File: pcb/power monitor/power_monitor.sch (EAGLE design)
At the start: 23 parts

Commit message: Signed-off-by: timcronin <tmpcronin@gmail.com>
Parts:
- removed C2: 10 uF, rcl:C-USC0805
- removed C3: 10 nF, rcl:C-USC0402
- removed C4: 22 uF, rcl:C-USC1206
- removed C5: 22 uF, rcl:C-USC0402
- removed C6: 100 nF, rcl:C-USC0402
- removed J1: (no value), con-jack:DCJ0303
- removed R1: 10K, rcl:R-US_R0603
- removed R5, R6: 500K, rcl:R-US_R0603
- removed U$1: MOMO-EDGE-SMALL-M, components:MOMO-EDGE-SMALL-M
- removed U$2: MOMO-EDGE-SMALL-F, components:MOMO-EDGE-SMALL-F
- removed U$3: MOMO-EDGE-POWER-M, components:MOMO-EDGE-POWER-M
- removed U$4: MOMO-EDGE-POWER-F, components:MOMO-EDGE-POWER-F
- removed U$8: 4.7 uH, components:NR6028-INDUCTOR
- removed U$9: MCP1702, components:MCP1702
- added IC1, IC2, IC3: MAX4105ESA, maxim:MAX4105ESA
- added R7: 1k, rcl:R-US_R0603
- added R8: 69.8k, rcl:R-US_R0603
- R2: value 100K -> 2
- R3: value 50K 1% -> 69.8k
- R4: value 13K 1% -> 1k
- U$6: value XRP7659 -> MOMO-EDGE-8F; device components:XRP7659 -> components:MOMO-EDGE-8F
- U$7: value DIODE_SS2P3 -> MOMO-EDGE-8M; device components:DIODE_SS2P3 -> components:MOMO-EDGE-8M
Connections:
- removed net +12V: C2.1, J1.1, R2.1, U$6.VIN
- removed net N$5: C6.1, R5.1, R6.2, U$5.RA4/AN3
- removed net N$6: R3.1, R4.2, U$6.FB
- new net N$11: IC2G$1.+IN, R2.1, U$7.2.8V
- new net N$7: IC3G$1.-IN, R3.2, R4.1
- new net N$9: IC3G$1.+IN, R7.1, R8.2
- net CLK: now also U$6.CLK, U$7.CLK; no longer U$1.SCL, U$2.SCL
- net DAT: now also U$6.DAT, U$7.DAT; no longer U$1.SDA, U$2.SDA
- net GND: now also IC1P.VEE, IC2P.VEE, IC3P.VEE, R8.1, U$6.PGND, U$7.GND, U$7.PGND; no longer C2.2, C4.2, C5.2, C6.2, J1.2, J1.3, R4.1, R6.1, U$1.GND, U$2.GND, U$7.AN, U$9.GND
- net IRQ: now also U$6.ALRM, U$7.ALRM; no longer U$1.IRQ, U$2.IRQ
- net N$1: now also U$6.NC, U$7.NC; no longer R1.2
- net N$2: now also IC3G$1.OUT, R3.1, U$5.RA4/AN3; no longer C3.2, U$6.SW, U$7.CATH, U$8.1
- net N$3: now also IC2G$1.-IN, IC2G$1.OUT, R4.2; no longer R2.2, U$6.EN
- net N$4: now also IC1G$1.-IN, IC1G$1.OUT, R7.2; no longer C3.1, U$6.BS
- net V+: now also IC3P.VCC, U$6.4V, U$7.4V; no longer C4.1, R3.2, R5.2, U$3.3.8V, U$4.3.8V, U$8.2, U$9.VIN
- net VCCINT: now also IC1G$1.+IN, IC1P.VCC, IC2P.VCC, R2.2, U$6.2.8V; no longer C5.1, R1.1, U$1.2.8V, U$2.2.8V, U$9.VOUT
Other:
- moved on the sheet: R2, R3, R4

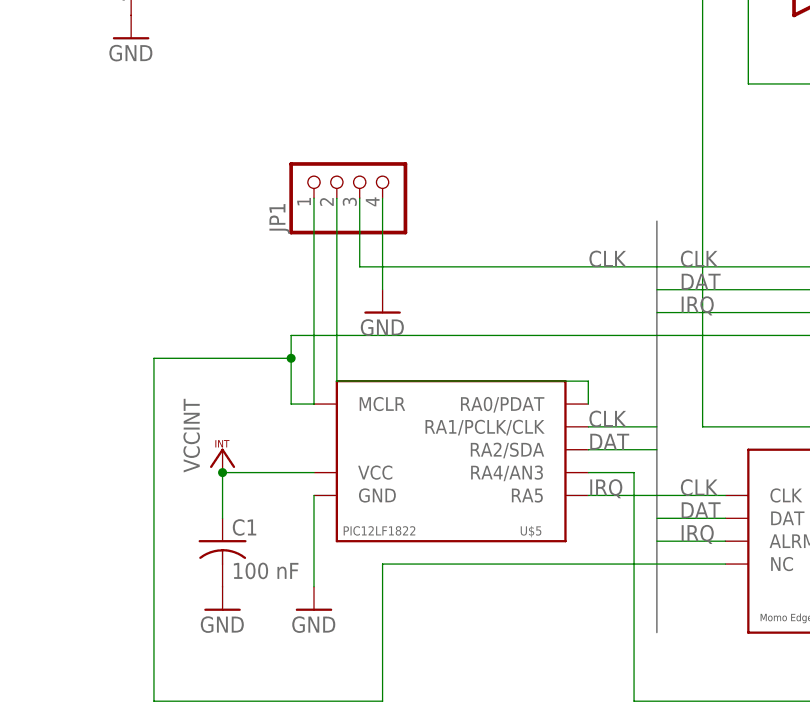
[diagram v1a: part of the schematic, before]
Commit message: Increased width of ground lines
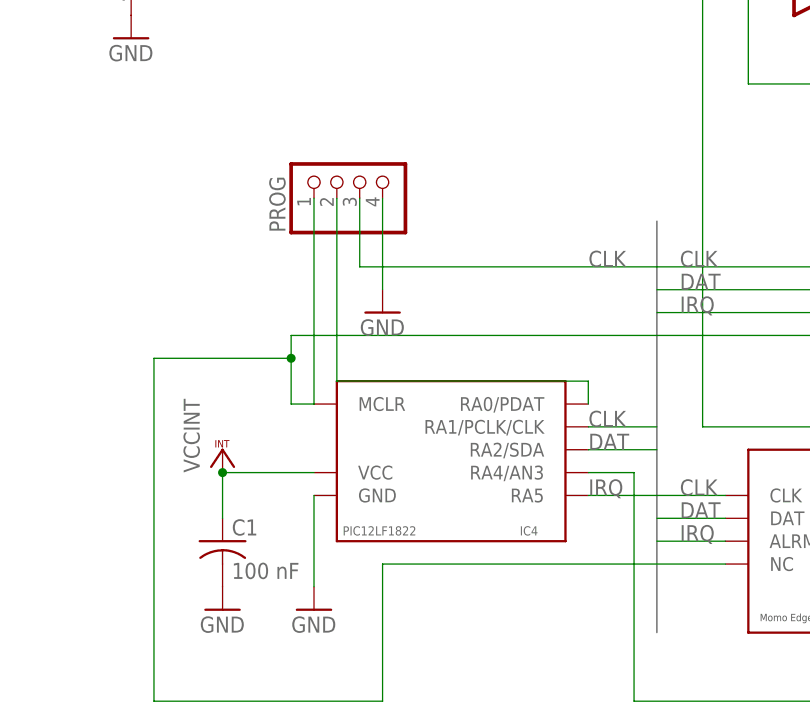
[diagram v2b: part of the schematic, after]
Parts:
- renumbered JP1 to PROG, U$5 to IC4
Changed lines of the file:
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@@
 </classes>
 <parts>
-<part name="U$5" library="components" deviceset="PIC12LF1822" device=""/>
+<part name="IC4" library="components" deviceset="PIC12LF1822" device=""/>
 <part name="VCC1" library="supply1" deviceset="VCCINT" device=""/>
 <part name="GND2" library="supply1" deviceset="GND" device=""/>
@@
 <part name="GND8" library="supply1" deviceset="GND" device=""/>
 <part name="GND9" library="supply1" deviceset="GND" device=""/>
-<part name="JP1" library="pinhead" deviceset="PINHD-1X4" device=""/>
+<part name="PROG" library="pinhead" deviceset="PINHD-1X4" device=""/>
 <part name="GND10" library="supply1" deviceset="GND" device=""/>
 <part name="IC1" library="maxim" deviceset="MAX4105ESA" device=""/>
@@
 </plain>
 <instances>
-<instance part="U$5" gate="G$1" x="-40.64" y="27.94"/>
+<instance part="IC4" gate="G$1" x="-40.64" y="27.94"/>
 <instance part="VCC1" gate="G$1" x="-55.88" y="22.86"/>
 <instance part="GND2" gate="1" x="-55.88" y="5.08"/>
@@
 <instance part="GND8" gate="1" x="38.1" y="20.32"/>
 <instance part="GND9" gate="1" x="12.7" y="-2.54"/>
-<instance part="JP1" gate="A" x="-40.64" y="53.34" rot="R90"/>
+<instance part="PROG" gate="A" x="-40.64" y="53.34" rot="R90"/>
 <instance part="GND10" gate="1" x="-38.1" y="38.1"/>
 <instance part="IC1" gate="G$1" x="12.7" y="96.52"/>
@@
 </segment>
 <segment>
-<pinref part="U$5" gate="G$1" pin="GND"/>
+<pinref part="IC4" gate="G$1" pin="GND"/>
 <pinref part="GND3" gate="1" pin="GND"/>
 <wire x1="-45.72" y1="17.78" x2="-45.72" y2="7.62" width="0.1524" layer="91"/>
 </segment>
 <segment>
-<pinref part="JP1" gate="A" pin="4"/>
+<pinref part="PROG" gate="A" pin="4"/>
 <pinref part="GND10" gate="1" pin="GND"/>
 <wire x1="-38.1" y1="40.64" x2="-38.1" y2="50.8" width="0.1524" layer="91"/>
@@
 <net name="N$1" class="0">
 <segment>
-<pinref part="U$5" gate="G$1" pin="MCLR"/>
+<pinref part="IC4" gate="G$1" pin="MCLR"/>
 <wire x1="-45.72" y1="27.94" x2="-45.72" y2="50.8" width="0.1524" layer="91"/>
-<pinref part="JP1" gate="A" pin="1"/>
+<pinref part="PROG" gate="A" pin="1"/>
 <pinref part="U$6" gate="G$1" pin="NC"/>
 <wire x1="25.4" y1="35.56" x2="-48.26" y2="35.56" width="0.1524" layer="91"/>
@@
 </segment>
 <segment>
-<pinref part="U$5" gate="G$1" pin="VCC"/>
+<pinref part="IC4" gate="G$1" pin="VCC"/>
 <pinref part="C1" gate="G$1" pin="1"/>
 <wire x1="-45.72" y1="20.32" x2="-55.88" y2="20.32" width="0.1524" layer="91"/>
@@
 </segment>
 <segment>
-<pinref part="U$5" gate="G$1" pin="RA1/PCLK/CLK"/>
+<pinref part="IC4" gate="G$1" pin="RA1/PCLK/CLK"/>
 <wire x1="-15.24" y1="25.4" x2="-7.62" y2="25.4" width="0.1524" layer="91"/>
 <label x="-15.24" y="25.4" size="1.778" layer="95"/>
@@
 <wire x1="-7.62" y1="43.18" x2="-40.64" y2="43.18" width="0.1524" layer="91"/>
 <label x="-15.24" y="43.18" size="1.778" layer="95"/>
-<pinref part="JP1" gate="A" pin="3"/>
+<pinref part="PROG" gate="A" pin="3"/>
 </segment>
 </net>
 <net name="DAT" class="0">
 <segment>
-<pinref part="U$5" gate="G$1" pin="RA2/SDA"/>
+<pinref part="IC4" gate="G$1" pin="RA2/SDA"/>
 <wire x1="-15.24" y1="22.86" x2="-7.62" y2="22.86" width="0.1524" layer="91"/>
 <label x="-15.24" y="22.86" size="1.778" layer="95"/>
@@
 <net name="IRQ" class="0">
 <segment>
-<pinref part="U$5" gate="G$1" pin="RA5"/>
+<pinref part="IC4" gate="G$1" pin="RA5"/>
 <wire x1="-15.24" y1="17.78" x2="-7.62" y2="17.78" width="0.1524" layer="91"/>
 <label x="-15.24" y="17.78" size="1.778" layer="95"/>
@@
 <net name="N$8" class="0">
 <segment>
-<pinref part="U$5" gate="G$1" pin="RA0/PDAT"/>
+<pinref part="IC4" gate="G$1" pin="RA0/PDAT"/>
 <wire x1="-15.24" y1="27.94" x2="-15.24" y2="30.48" width="0.1524" layer="91"/>
 <wire x1="-15.24" y1="30.48" x2="-43.18" y2="30.48" width="0.1524" layer="91"/>
 <wire x1="-43.18" y1="30.48" x2="-43.18" y2="50.8" width="0.1524" layer="91"/>
-<pinref part="JP1" gate="A" pin="2"/>
+<pinref part="PROG" gate="A" pin="2"/>
 </segment>
 </net>
@@
 <pinref part="R3" gate="G$1" pin="1"/>
 <wire x1="68.58" y1="71.12" x2="63.5" y2="71.12" width="0.1524" layer="91"/>
-<pinref part="U$5" gate="G$1" pin="RA4/AN3"/>
+<pinref part="IC4" gate="G$1" pin="RA4/AN3"/>
 <wire x1="-15.24" y1="20.32" x2="-10.16" y2="20.32" width="0.1524" layer="91"/>
 <wire x1="-10.16" y1="20.32" x2="-10.16" y2="-5.08" width="0.1524" layer="91"/>
